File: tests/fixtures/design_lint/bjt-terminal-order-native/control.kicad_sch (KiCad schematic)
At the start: 4 parts, among them Q1 Synthetic NPN, Q2 Synthetic PNP, U1 NPN base driver, U2 PNP base driver

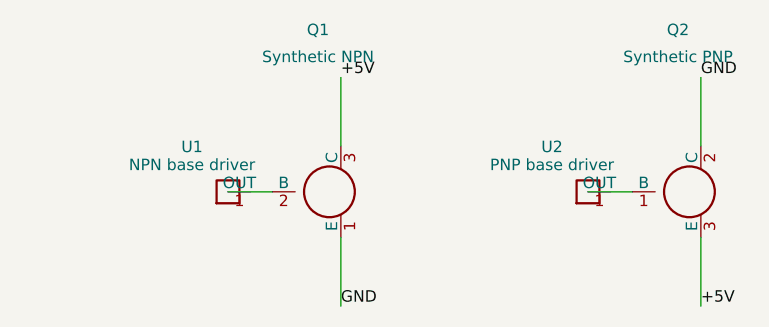
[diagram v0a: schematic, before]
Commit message: test: add native BJT base-drive evidence gate
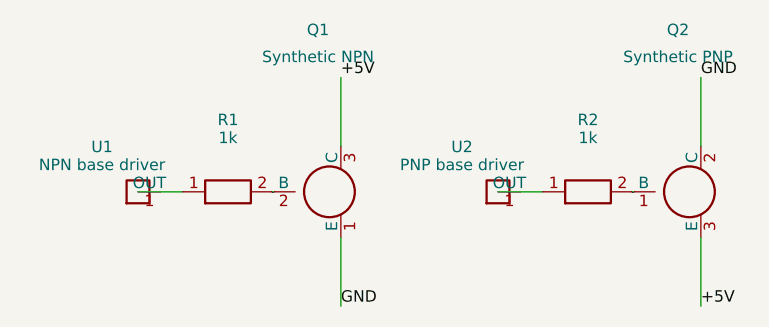
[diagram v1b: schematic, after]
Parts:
- added R1, R2: 1k, Synthetic:R_0603, symbol Device:R
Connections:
- net at Q1.2 (B): now also R1.2; no longer U1.1 (OUT)
- net at Q2.1 (B): now also R2.2; no longer U2.1 (OUT)
- new net: R1.1, U1.1 (OUT)
- new net: R2.1, U2.1 (OUT)
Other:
- title: Synthetic BJT collector emitter order control -> Synthetic BJT rail-order and series-base-resistor control
- moved on the sheet: U1, U2
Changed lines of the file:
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@@
 (kicad_sch (version 20231120) (generator "eeschema")
   (paper "A4")
-  (title_block (title "Synthetic BJT collector emitter order control")
+  (title_block (title "Synthetic BJT rail-order and series-base-resistor control")
     (comment 1 "NOT FOR MANUFACTURE - tooling fixture"))
   (symbol (lib_id "Transistor_BJT:Q_NPN_EBC") (at 100 100 0) (unit 1)
@@
     (instances (project "Synthetic BJT control"
       (path "/56000000-0000-4000-8000-000000000301" (reference "Q2") (unit 1)))))
-  (symbol (lib_id "Synthetic:Drive_OUT") (at 90 100 0) (unit 1)
+  (symbol (lib_id "Synthetic:Drive_OUT") (at 80 100 0) (unit 1)
     (in_bom yes) (on_board yes) (dnp no)
-    (property "Reference" "U1" (at 86 95 0) (effects (font (size 1.27 1.27))))
-    (property "Value" "NPN base driver" (at 86 97 0) (effects (font (size 1.27 1.27))))
-    (property "Footprint" "" (at 90 100 0) (effects (font (size 1.27 1.27)) hide))
+    (property "Reference" "U1" (at 76 95 0) (effects (font (size 1.27 1.27))))
+    (property "Value" "NPN base driver" (at 76 97 0) (effects (font (size 1.27 1.27))))
+    (property "Footprint" "" (at 80 100 0) (effects (font (size 1.27 1.27)) hide))
     (pin "1")
     (instances (project "Synthetic BJT control"
       (path "/56000000-0000-4000-8000-000000000301" (reference "U1") (unit 1)))))
-  (symbol (lib_id "Synthetic:Drive_OUT") (at 130 100 0) (unit 1)
+  (symbol (lib_id "Synthetic:Drive_OUT") (at 120 100 0) (unit 1)
     (in_bom yes) (on_board yes) (dnp no)
-    (property "Reference" "U2" (at 126 95 0) (effects (font (size 1.27 1.27))))
-    (property "Value" "PNP base driver" (at 126 97 0) (effects (font (size 1.27 1.27))))
-    (property "Footprint" "" (at 130 100 0) (effects (font (size 1.27 1.27)) hide))
+    (property "Reference" "U2" (at 116 95 0) (effects (font (size 1.27 1.27))))
+    (property "Value" "PNP base driver" (at 116 97 0) (effects (font (size 1.27 1.27))))
+    (property "Footprint" "" (at 120 100 0) (effects (font (size 1.27 1.27)) hide))
     (pin "1")
     (instances (project "Synthetic BJT control"
       (path "/56000000-0000-4000-8000-000000000301" (reference "U2") (unit 1)))))
-  (wire (pts (xy 90 100) (xy 94.92 100))
+  (symbol (lib_id "Device:R") (at 90 100 0) (unit 1)
+    (in_bom yes) (on_board yes) (dnp no)
+    (property "Reference" "R1" (at 90 92 0) (effects (font (size 1.27 1.27))))
+    (property "Value" "1k" (at 90 94 0) (effects (font (size 1.27 1.27))))
+    (property "Footprint" "Synthetic:R_0603" (at 90 100 0) (effects (font (size 1.27 1.27)) hide))
+    (property "Datasheet" "" (at 90 100 0) (effects (font (size 1.27 1.27)) hide))
+    (pin "1")
+    (pin "2")
+    (instances (project "Synthetic BJT control"
+      (path "/56000000-0000-4000-8000-000000000301" (reference "R1") (unit 1)))))
+  (symbol (lib_id "Device:R") (at 130 100 0) (unit 1)
+    (in_bom yes) (on_board yes) (dnp no)
+    (property "Reference" "R2" (at 130 92 0) (effects (font (size 1.27 1.27))))
+    (property "Value" "1k" (at 130 94 0) (effects (font (size 1.27 1.27))))
+    (property "Footprint" "Synthetic:R_0603" (at 130 100 0) (effects (font (size 1.27 1.27)) hide))
+    (property "Datasheet" "" (at 130 100 0) (effects (font (size 1.27 1.27)) hide))
+    (pin "1")
+    (pin "2")
+    (instances (project "Synthetic BJT control"
+      (path "/56000000-0000-4000-8000-000000000301" (reference "R2") (unit 1)))))
+  (wire (pts (xy 80 100) (xy 84.92 100))
     (stroke (width 0) (type default)))
-  (wire (pts (xy 130 100) (xy 134.92 100))
+  (wire (pts (xy 95.08 100) (xy 94.92 100))
+    (stroke (width 0) (type default)))
+  (wire (pts (xy 120 100) (xy 124.92 100))
+    (stroke (width 0) (type default)))
+  (wire (pts (xy 135.08 100) (xy 134.92 100))
     (stroke (width 0) (type default)))
   (wire (pts (xy 102.54 94.92) (xy 102.54 87.3))
